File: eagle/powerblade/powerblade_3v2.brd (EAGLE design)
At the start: 25.4 x 25.4 mm, 79 parts, among them J1 JTAG_14PIN_IDC-ND, J2 AC_INF4, J4 TC2030-JLINK-NL, Q1 NTS4173, Q4 2SK1829, U1 TPS62122, U2 MCP6V3, U3 MSP430FR5738, U4 NRF51822QF, U6 MAX9910, U7 OPA2369, X1 16MHz, X3 32.768kHz, Y1 UREACH_XTEND

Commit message: updated l41
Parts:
- J2: value AC_INF4 -> AC_INF41; device powerfilm:AC3_F4 -> powerfilm:AC3_F41
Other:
- outline, holes or cut-outs redrawn
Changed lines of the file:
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@@
 <?xml version="1.0" encoding="utf-8"?>
 <!DOCTYPE eagle SYSTEM "eagle.dtd">
-<eagle version="6.5.0">
+<eagle version="6.3">
 <drawing>
 <settings>
@@
 <attribute name="DIGIKEY" value="490-4025-1-ND" x="4.727575" y="-16.002" size="1.778" layer="27" rot="R270" display="off"/>
 </element>
-<element name="J2" library="powerfilm" package="AC3_F4" value="AC_INF4" x="0" y="0">
+<element name="J2" library="powerfilm" package="AC3_F41" value="AC_INF41" x="0" y="0">
 <attribute name="DIGIKEY" value="ED1649-ND" x="0" y="0" size="1.778" layer="27" display="off"/>
 <attribute name="DIGIKEY_2" value="ED1649-ND" x="0" y="0" size="1.778" layer="27" display="off"/>
@@
 </signal>
 </signals>
-<errors>
-</errors>
 </board>
 </drawing>

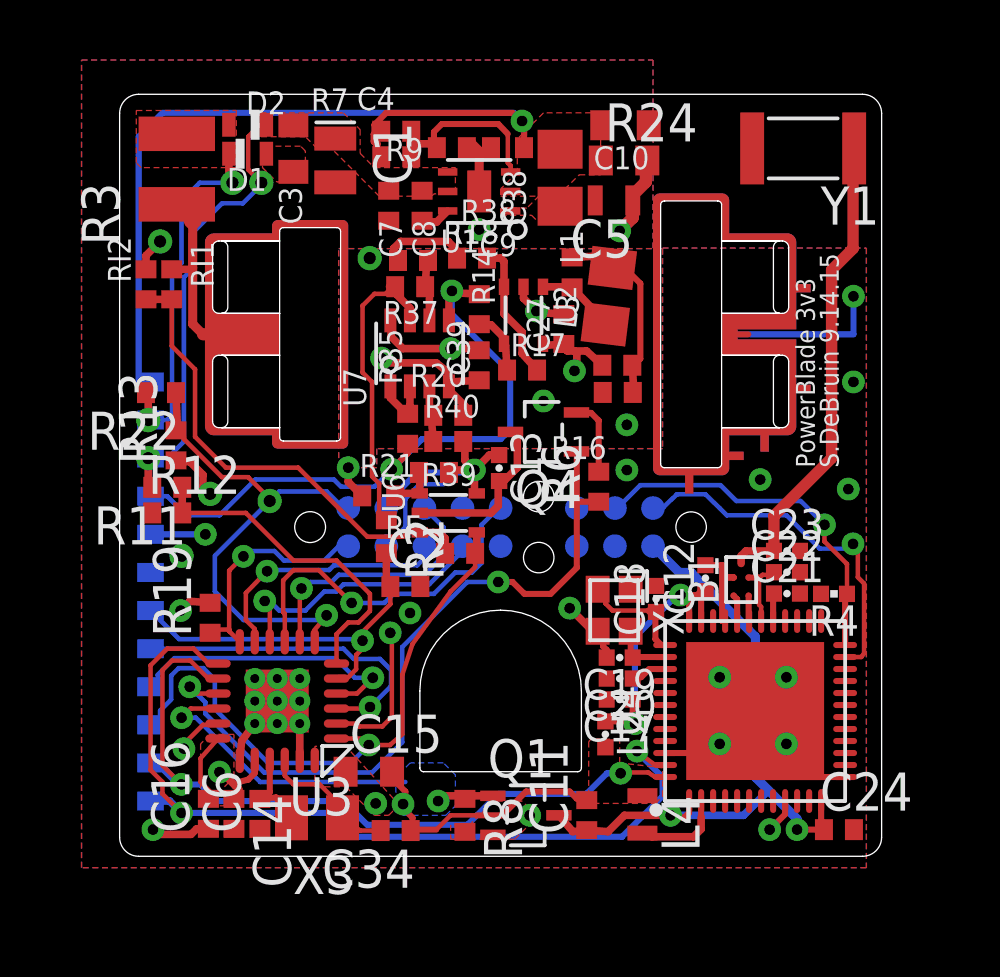
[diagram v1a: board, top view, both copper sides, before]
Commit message: updated plating not around the whole cutout
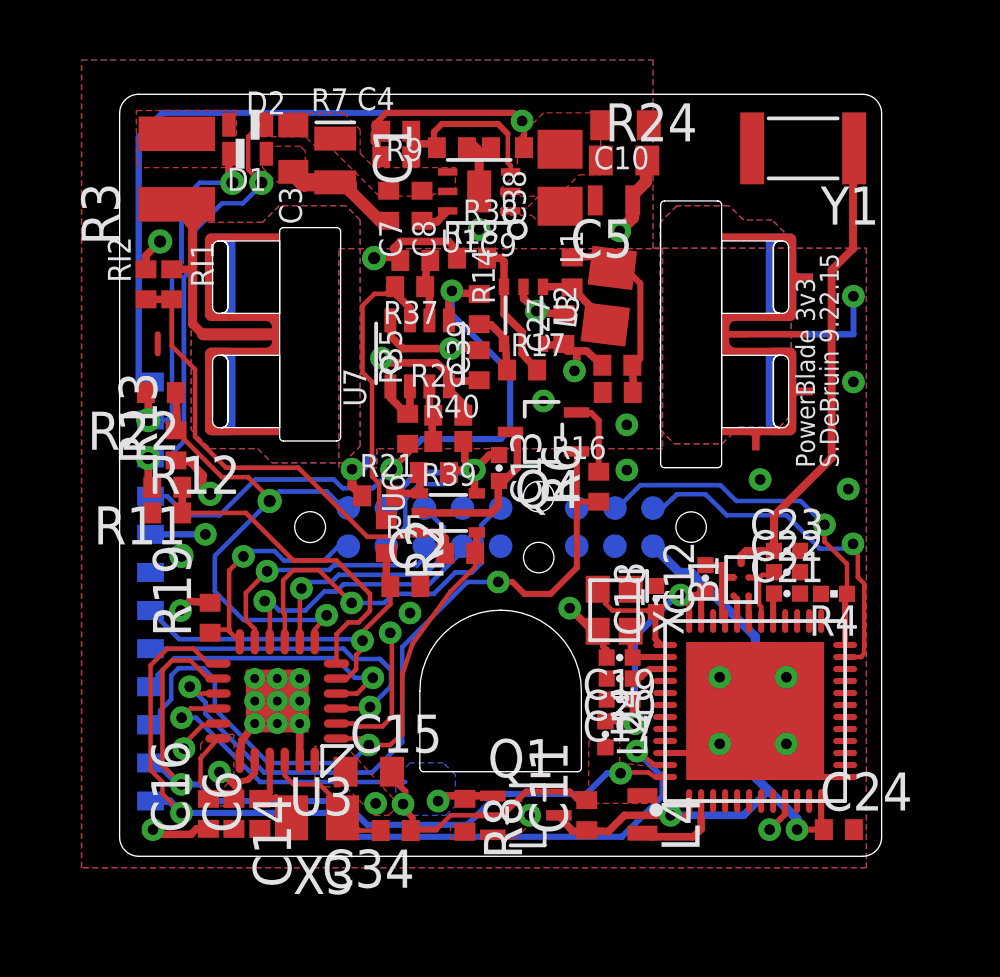
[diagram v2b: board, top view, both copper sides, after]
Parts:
- moved R38 0.08 mm to (-2.84, 2.46)
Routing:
- net GND: track 45.5 -> 52.2 mm
- net GND3: track 27.1 -> 28.8 mm
- net TEMP: track 0.00 -> 0.64 mm
- added copper zone on layer 1, net TEMP
- added copper zone on layer 15, net TEMP
- added copper zone on layer 16, net TEMP
- added copper zone on layer 2, net TEMP
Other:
- board text added: "S.DeBruin 9.22.15"
- board text removed: "S.DeBruin 9.14.15"

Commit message: updated board? I hope i dont get conflicts
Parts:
- J2: value AC_INF41 -> AC_INF45; device powerfilm:AC3_F41 -> powerfilm:AC3_F45
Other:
- outline, holes or cut-outs redrawn
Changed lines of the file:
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@@
 <attribute name="DIGIKEY" value="490-4025-1-ND" x="4.727575" y="-16.002" size="1.778" layer="27" rot="R270" display="off"/>
 </element>
-<element name="J2" library="powerfilm" package="AC3_F41" value="AC_INF41" x="0" y="0">
+<element name="J2" library="powerfilm" package="AC3_F45" value="AC_INF45" x="0" y="0">
 <attribute name="DIGIKEY" value="ED1649-ND" x="0" y="0" size="1.778" layer="27" display="off"/>
 <attribute name="DIGIKEY_2" value="ED1649-ND" x="0" y="0" size="1.778" layer="27" display="off"/>
